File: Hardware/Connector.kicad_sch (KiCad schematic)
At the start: 14 parts, among them J1 XIAO ESP32S3 Sense, J2 Conn_02x16_Counter_Clockwise, J3 FTSH-107-01-L-D-K

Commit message: Added Tensionmeters initial version
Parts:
- F6: Mouser Part Number . -> 603-SMD0603B010TF
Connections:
- net +12V: now reaches J2.15 (Pin_15)
- net Tens_Out1+: now reaches J2.4 (Pin_4)
- net Tens_Out1-: now reaches J2.5 (Pin_5)
- net Tens_Out2+: now reaches J2.6 (Pin_6)
- net Tens_Out2-: now reaches J2.7 (Pin_7)
- no-connect marks 21 -> 16
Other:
- note removed: "1: Signals with no connect flag are still on Connector but are not proccesed on this board"
- note removed: "STEERING_POSITION_2_IN"
- note removed: "STEERING_POSITION_IN"
- note removed: "SUSPENSION_POT1_IN"
- note removed: "SUSPENSION_POT2_IN"
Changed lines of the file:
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@@
 		)
 	)
-	(text "1: 	Signals with no connect flag are still on Connector\n	but are not proccesed on this board\n"
-		(exclude_from_sim no)
-		(at 29.21 97.79 0)
-		(effects
-			(font
-				(size 1.27 1.27)
-			)
-			(justify left)
-		)
-	)
 	(text "1*"
 		(exclude_from_sim no)
@@
 		)
 	)
-	(text "1*"
-		(exclude_from_sim no)
-		(at 86.36 83.82 0)
-		(effects
-			(font
-				(size 1.27 1.27)
-			)
-		)
-	)
-	(text "SUSPENSION_POT1_IN"
-		(exclude_from_sim no)
-		(at 95.25 81.28 0)
-		(effects
-			(font
-				(size 1.27 1.27)
-			)
-			(justify left bottom)
-		)
-	)
-	(text "SUSPENSION_POT2_IN"
-		(exclude_from_sim no)
-		(at 95.25 86.36 0)
-		(effects
-			(font
-				(size 1.27 1.27)
-			)
-			(justify left bottom)
-		)
-	)
-	(text "STEERING_POSITION_IN"
-		(exclude_from_sim no)
-		(at 93.98 83.82 0)
-		(effects
-			(font
-				(size 1.27 1.27)
-			)
-			(justify left bottom)
-		)
-	)
-	(text "STEERING_POSITION_2_IN"
-		(exclude_from_sim no)
-		(at 91.44 88.9 0)
-		(effects
-			(font
-				(size 1.27 1.27)
-			)
-			(justify left bottom)
-		)
-	)
 	(junction
 		(at 132.08 116.84)
@@
 	)
 	(no_connect
-		(at 116.84 82.55)
-	)
-	(no_connect
 		(at 261.62 52.07)
 	)
@@
 	)
 	(no_connect
-		(at 116.84 87.63)
-	)
-	(no_connect
 		(at 261.62 49.53)
 	)
@@
 	)
 	(no_connect
-		(at 116.84 80.01)
-	)
-	(no_connect
-		(at 116.84 85.09)
-	)
-	(no_connect
 		(at 238.76 46.99)
 	)
@@
 	)
 	(no_connect
-		(at 116.84 107.95)
-	)
-	(no_connect
 		(at 207.01 106.68)
 	)
@@
 		)
 	)
-	(polyline
+	(wire
 		(pts
-			(xy 88.9 88.9) (xy 91.44 88.9)
+			(xy 204.47 111.76) (xy 207.01 111.76)
 		)
 		(stroke
@@
 	(wire
 		(pts
-			(xy 204.47 111.76) (xy 207.01 111.76)
+			(xy 113.03 74.93) (xy 116.84 74.93)
 		)
 		(stroke
@@
 		)
 	)
-	(wire
+	(polyline
 		(pts
-			(xy 113.03 74.93) (xy 116.84 74.93)
+			(xy 105.41 106.68) (xy 107.95 106.68)
 		)
 		(stroke
@@
 		)
 	)
-	(polyline
+	(wire
 		(pts
-			(xy 105.41 106.68) (xy 107.95 106.68)
+			(xy 266.7 41.91) (xy 266.7 43.18)
 		)
 		(stroke
@@
 	(wire
 		(pts
-			(xy 266.7 41.91) (xy 266.7 43.18)
+			(xy 113.03 87.63) (xy 116.84 87.63)
 		)
 		(stroke
@@
 		)
 	)
+	(wire
+		(pts
+			(xy 113.03 107.95) (xy 116.84 107.95)
+		)
+		(stroke
+			(width 0)
+			(type default)
+		)
+	)
 	(bus
 		(pts
@@
 		)
 	)
-	(bus
+	(wire
 		(pts
-			(xy 132.08 116.84) (xy 154.94 116.84)
+			(xy 113.03 80.01) (xy 116.84 80.01)
 		)
 		(stroke
@@
 		)
 	)
-	(wire
+	(bus
 		(pts
-			(xy 129.54 92.71) (xy 166.37 92.71)
+			(xy 132.08 116.84) (xy 154.94 116.84)
 		)
 		(stroke
@@
 	(wire
 		(pts
-			(xy 245.11 147.32) (xy 245.11 151.13)
+			(xy 129.54 92.71) (xy 166.37 92.71)
 		)
 		(stroke
@@
 		)
 	)
-	(bus
+	(wire
 		(pts
-			(xy 240.03 106.68) (xy 240.03 111.76)
+			(xy 245.11 147.32) (xy 245.11 151.13)
 		)
 		(stroke
@@
 		)
 	)
-	(polyline
+	(bus
 		(pts
-			(xy 91.44 78.74) (xy 88.9 78.74)
+			(xy 240.03 106.68) (xy 240.03 111.76)
 		)
 		(stroke
@@
 	(polyline
 		(pts
-			(xy 88.9 78.74) (xy 88.9 88.9)
-		)
-		(stroke
-			(width 0)
-			(type default)
-		)
-	)
-	(polyline
-		(pts
 			(xy 105.41 106.68) (xy 105.41 101.6)
 		)
@@
 	(wire
 		(pts
+			(xy 113.03 82.55) (xy 116.84 82.55)
+		)
+		(stroke
+			(width 0)
+			(type default)
+		)
+	)
+	(wire
+		(pts
 			(xy 171.45 95.25) (xy 171.45 93.98)
 		)
@@
 	(wire
 		(pts
+			(xy 113.03 85.09) (xy 116.84 85.09)
+		)
+		(stroke
+			(width 0)
+			(type default)
+		)
+	)
+	(wire
+		(pts
 			(xy 195.58 72.39) (xy 200.66 72.39)
 		)
@@
 		)
 	)
+	(hierarchical_label "Tens_Out1-"
+		(shape input)
+		(at 113.03 82.55 180)
+		(effects
+			(font
+				(size 1.27 1.27)
+			)
+			(justify right)
+		)
+	)
 	(hierarchical_label "APPS_POT_1"
 		(shape output)
@@
 		)
 	)
+	(hierarchical_label "Tens_Out2-"
+		(shape input)
+		(at 113.03 87.63 180)
+		(effects
+			(font
+				(size 1.27 1.27)
+			)
+			(justify right)
+		)
+	)
 	(hierarchical_label "GND_CAN_ISO1"
 		(shape input)
@@
 		)
 	)
+	(hierarchical_label "Tens_Out2+"
+		(shape input)
+		(at 113.03 85.09 180)
+		(effects
+			(font
+				(size 1.27 1.27)
+			)
+			(justify right)
+		)
+	)
 	(hierarchical_label "BRAKE_PRESSURE2_IN"
 		(shape output)
@@
 		)
 	)
+	(hierarchical_label "Tens_Out1+"
+		(shape input)
+		(at 113.03 80.01 180)
+		(effects
+			(font
+				(size 1.27 1.27)
+			)
+			(justify right)
+		)
+	)
 	(hierarchical_label "UART_TX_PROG"
 		(shape input)
@@
 			)
 		)
-		(property "Mouser Part Number" "."
+		(property "Mouser Part Number" "603-SMD0603B010TF"
 			(at 144.78 72.39 0)
 			(effects
@@
 					(size 1.27 1.27)
 				)
+				(hide yes)
 			)
 		)
@@
 					(unit 1)
 				)
+			)
+		)
+	)
+	(symbol
+		(lib_id "power:+12V")
+		(at 113.03 107.95 90)
+		(unit 1)
+		(exclude_from_sim no)
+		(in_bom yes)
+		(on_board yes)
+		(dnp no)
+		(fields_autoplaced yes)
+		(property "Reference" "#PWR09"
+			(at 116.84 107.95 0)
+			(effects
+				(font
+					(size 1.27 1.27)
+				)
+				(hide yes)
+			)
+		)
+		(property "Value" "+12V"
+			(at 109.22 107.9499 90)
+			(effects
+				(font
+					(size 1.27 1.27)
+				)
+				(justify left)
+			)
+		)
+		(property "Footprint" ""
+			(at 113.03 107.95 0)
+			(effects
+				(font
+					(size 1.27 1.27)
+				)
+				(hide yes)
+			)
+		)
+		(property "Datasheet" ""
+			(at 113.03 107.95 0)
+			(effects
+				(font
+					(size 1.27 1.27)
+				)
+				(hide yes)
+			)
+		)
+		(property "Description" "Power symbol creates a global label with name \"+12V\""
+			(at 113.03 107.95 0)
+			(effects
+				(font
+					(size 1.27 1.27)
+				)
+				(hide yes)
+			)
+		)
+		(pin "1"
+		)
+		(instances
+			(project ""
+				(path "/b652b05a-4e3d-4ad1-b032-18886abe7d45/05ab4043-b566-4501-8a33-377ac21fdb45"
+					(reference "#PWR09")
+					(unit 1)
+				)

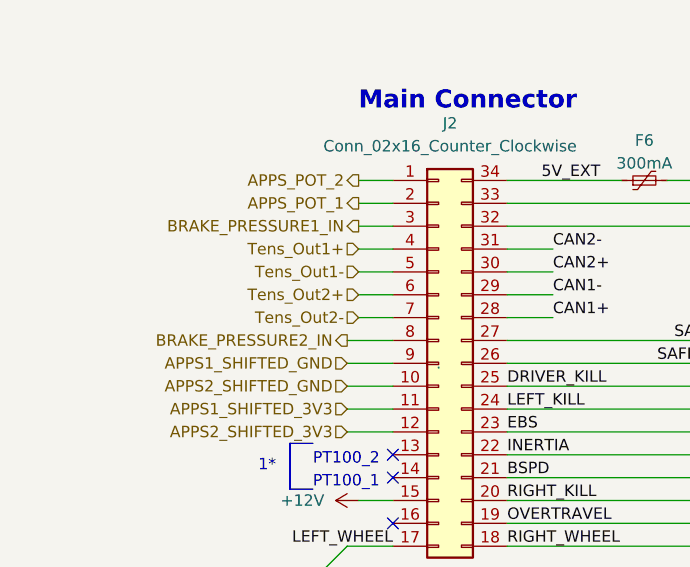
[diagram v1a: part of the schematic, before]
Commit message: Added tensionmeter section, updated APPS resistors for transfer function
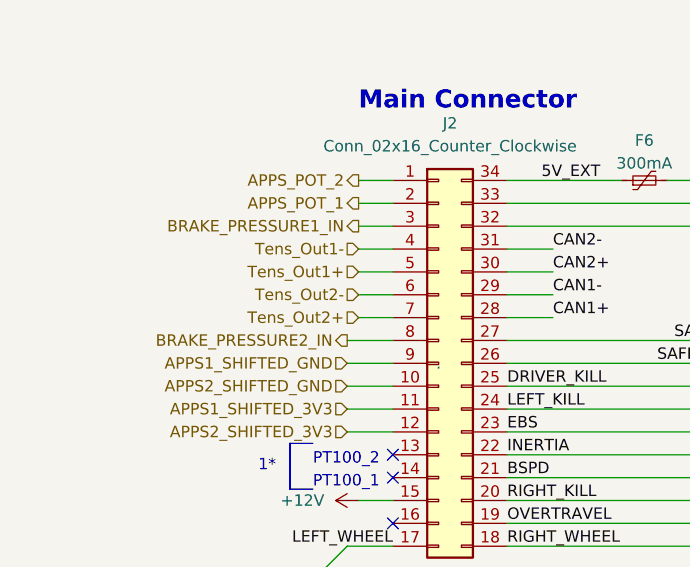
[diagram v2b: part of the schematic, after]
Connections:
- net Tens_Out1+: now also J2.5 (Pin_5); no longer J2.4 (Pin_4)
- net Tens_Out1-: now also J2.4 (Pin_4); no longer J2.5 (Pin_5)
- net Tens_Out2+: now also J2.7 (Pin_7); no longer J2.6 (Pin_6)
- net Tens_Out2-: now also J2.6 (Pin_6); no longer J2.7 (Pin_7)
